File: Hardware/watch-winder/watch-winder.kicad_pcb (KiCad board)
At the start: 2 copper layers, 53 parts, among them J1 SWD, J2 UART, J3 MOT, J4 SYNC0, J5 SYNC1, J6 PWR, SW1 SW_Push, SW2 SW_Push, SW3 SW_Push, U1 STM32F030K6Tx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

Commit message: add pcb cutout, set 4 layer stackup
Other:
- board outline added: 50 x 50 mm
- copper layers 2 -> 4
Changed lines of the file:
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@@
 	(layers
 		(0 "F.Cu" signal)
+		(4 "In1.Cu" signal)
+		(6 "In2.Cu" signal)
 		(2 "B.Cu" signal)
 		(9 "F.Adhes" user "F.Adhesive")
@@
 	)
 	(setup
+		(stackup
+			(layer "F.SilkS"
+				(type "Top Silk Screen")
+			)
+			(layer "F.Paste"
+				(type "Top Solder Paste")
+			)
+			(layer "F.Mask"
+				(type "Top Solder Mask")
+				(thickness 0.01)
+			)
+			(layer "F.Cu"
+				(type "copper")
+				(thickness 0.035)
+			)
+			(layer "dielectric 1"
+				(type "prepreg")
+				(thickness 0.21)
+				(material "FR4")
+				(epsilon_r 4.5)
+				(loss_tangent 0.02)
+			)
+			(layer "In1.Cu"
+				(type "copper")
+				(thickness 0.015)
+			)
+			(layer "dielectric 2"
+				(type "core")
+				(thickness 1.06)
+				(material "FR4")
+				(epsilon_r 4.5)
+				(loss_tangent 0.02)
+			)
+			(layer "In2.Cu"
+				(type "copper")
+				(thickness 0.015)
+			)
+			(layer "dielectric 3"
+				(type "prepreg")
+				(thickness 0.21)
+				(material "FR4")
+				(epsilon_r 4.5)
+				(loss_tangent 0.02)
+			)
+			(layer "B.Cu"
+				(type "copper")
+				(thickness 0.035)
+			)
+			(layer "B.Mask"
+				(type "Bottom Solder Mask")
+				(thickness 0.01)
+			)
+			(layer "B.Paste"
+				(type "Bottom Solder Paste")
+			)
+			(layer "B.SilkS"
+				(type "Bottom Silk Screen")
+			)
+			(copper_finish "None")
+			(dielectric_constraints no)
+		)
 		(pad_to_mask_clearance 0)
 		(allow_soldermask_bridges_in_footprints no)
@@
 		)
 	)
+	(gr_rect
+		(start 160 100)
+		(end 210 150)
+		(stroke
+			(width 0.05)
+			(type default)
+		)
+		(fill no)
+		(layer "Edge.Cuts")
+	)
 	(embedded_fonts no)

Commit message: add gnd planes
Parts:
- moved J1 4.44 mm to (227.9, 102.7)
- moved J2 4.44 mm to (227.9, 114.9)
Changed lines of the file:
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@@
 	(footprint "Connector_PinHeader_2.54mm:PinHeader_1x04_P2.54mm_Horizontal"
 		(layer "F.Cu")
-		(at 227.87 119.355)
+		(at 227.87 114.92)
 		(descr "Through hole angled pin header, 1x04, 2.54mm pitch, 6mm pin length, single row")
 		(tags "Through hole angled pin header THT 1x04 2.54mm single row")
@@
 	(footprint "Connector_PinHeader_2.54mm:PinHeader_1x04_P2.54mm_Horizontal"
 		(layer "F.Cu")
-		(at 227.87 107.105)
+		(at 227.87 102.67)
 		(descr "Through hole angled pin header, 1x04, 2.54mm pitch, 6mm pin length, single row")
 		(tags "Through hole angled pin header THT 1x04 2.54mm single row")
@@
 	)
 	(gr_rect
+		(start 160 100)
+		(end 210 150)
+		(stroke
+			(width 0.2)
+			(type solid)
+		)
+		(fill yes)
+		(layer "In1.Cu")
+		(net 1)
+	)
+	(gr_rect
+		(start 160 100)
+		(end 210 150)
+		(stroke
+			(width 0.2)
+			(type solid)
+		)
+		(fill yes)
+		(layer "In2.Cu")
+		(net 1)
+	)
+	(gr_rect

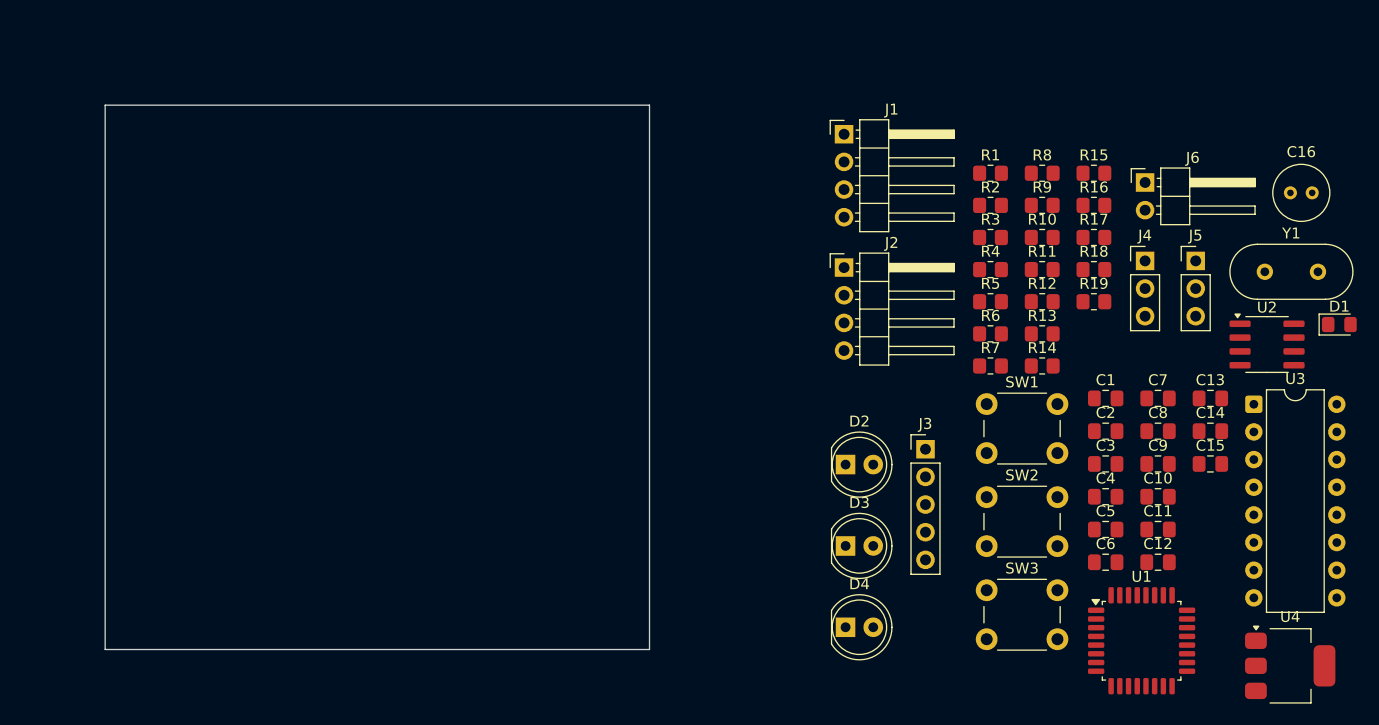
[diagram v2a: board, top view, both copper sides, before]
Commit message: start button/led placement
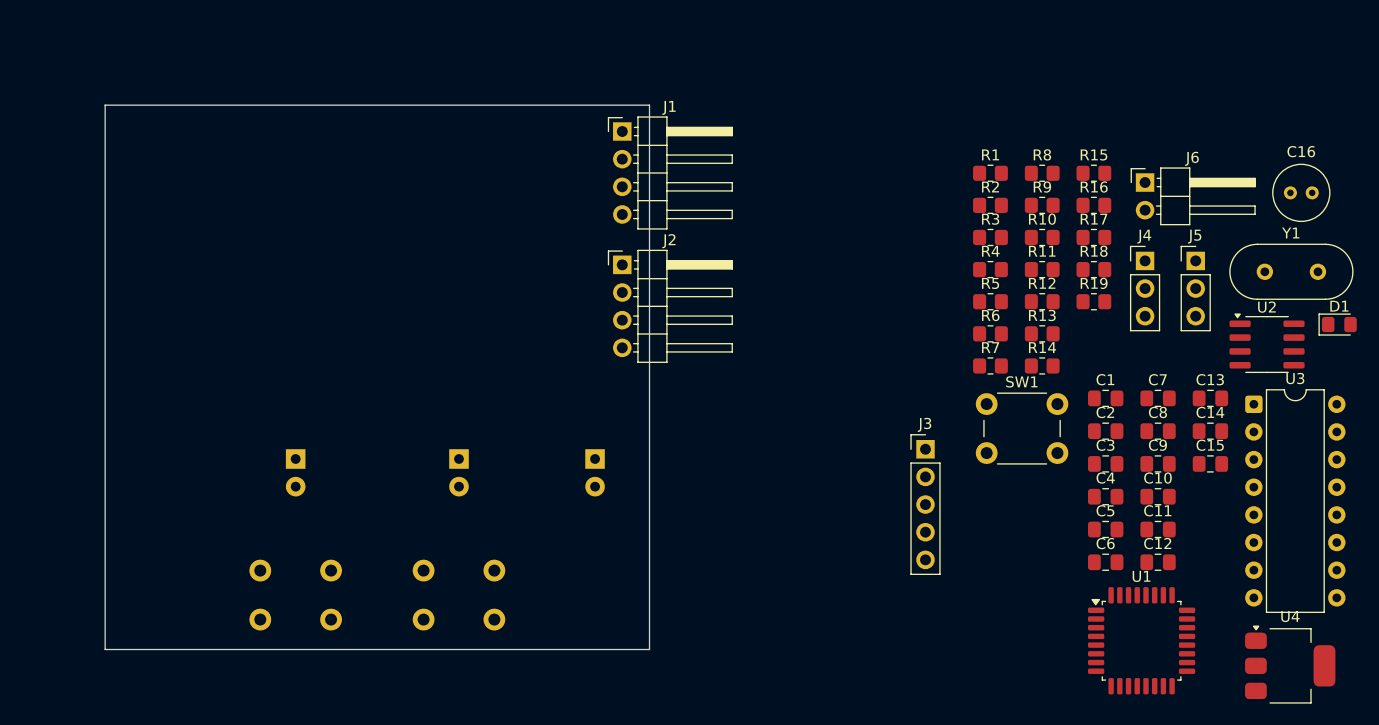
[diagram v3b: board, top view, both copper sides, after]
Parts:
- D2, D3, D4, SW2, SW3: moved to B.Cu
- moved SW3 66.8 mm to (174.2, 147.2)
- moved SW2 52.9 mm to (189.2, 147.2)
- moved D2 50.5 mm to (177.5, 132.5), turned to -90 degrees
- moved D3 36.4 mm to (192.5, 132.5), turned to -90 degrees
- moved D4 27.7 mm to (205.0, 132.5), turned to -90 degrees
- moved J1 20.4 mm to (207.5, 102.4)
- moved J2 20.4 mm to (207.5, 114.7)

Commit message: fix gnd, more components
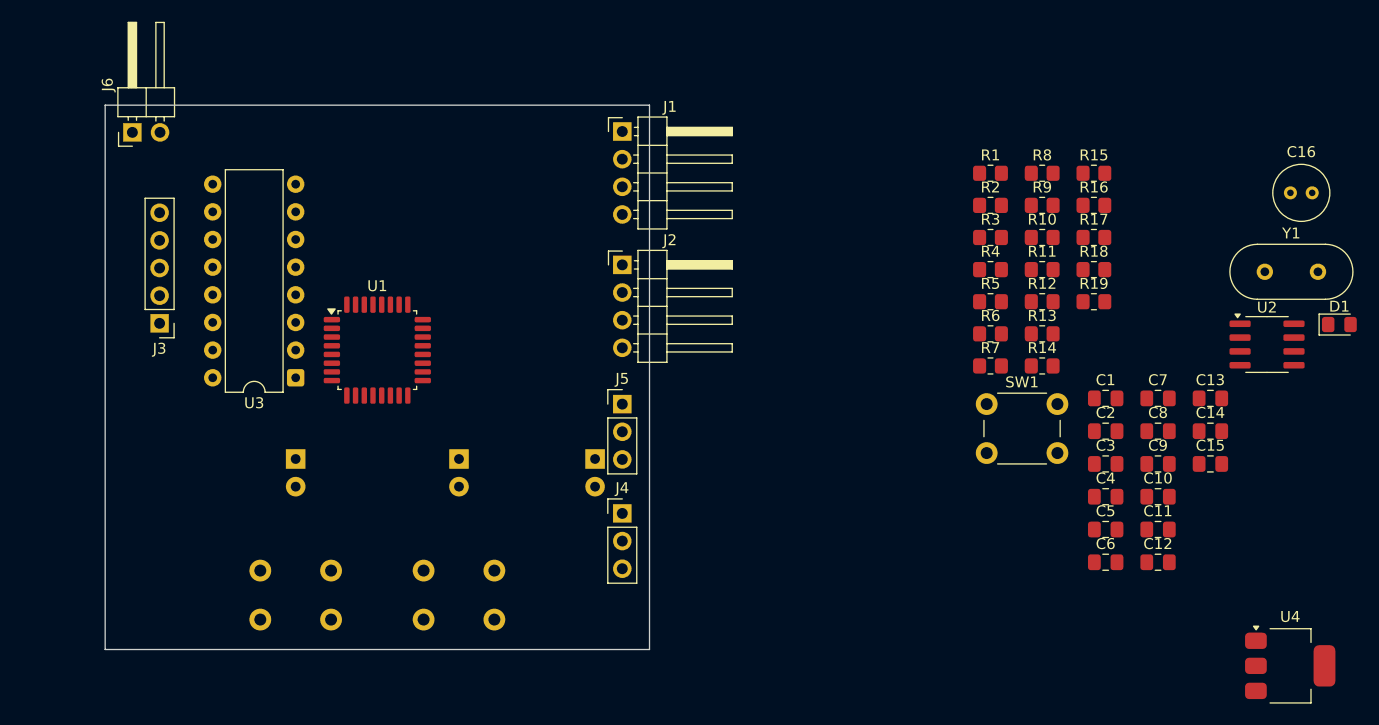
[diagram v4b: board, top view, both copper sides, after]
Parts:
- moved J6 93.1 mm to (162.5, 102.5), turned to 90 degrees
- moved U3 88.0 mm to (177.5, 125.0), turned to 180 degrees
- moved U1 75.1 mm to (185.0, 122.5)
- moved J3 71.3 mm to (165.0, 120.0), turned to 180 degrees
- moved J5 54.3 mm to (207.5, 127.5)
- moved J4 53.3 mm to (207.5, 137.5)
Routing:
- added copper zone on In1.Cu, net GND
- added copper zone on In2.Cu, net GND

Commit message: better placement
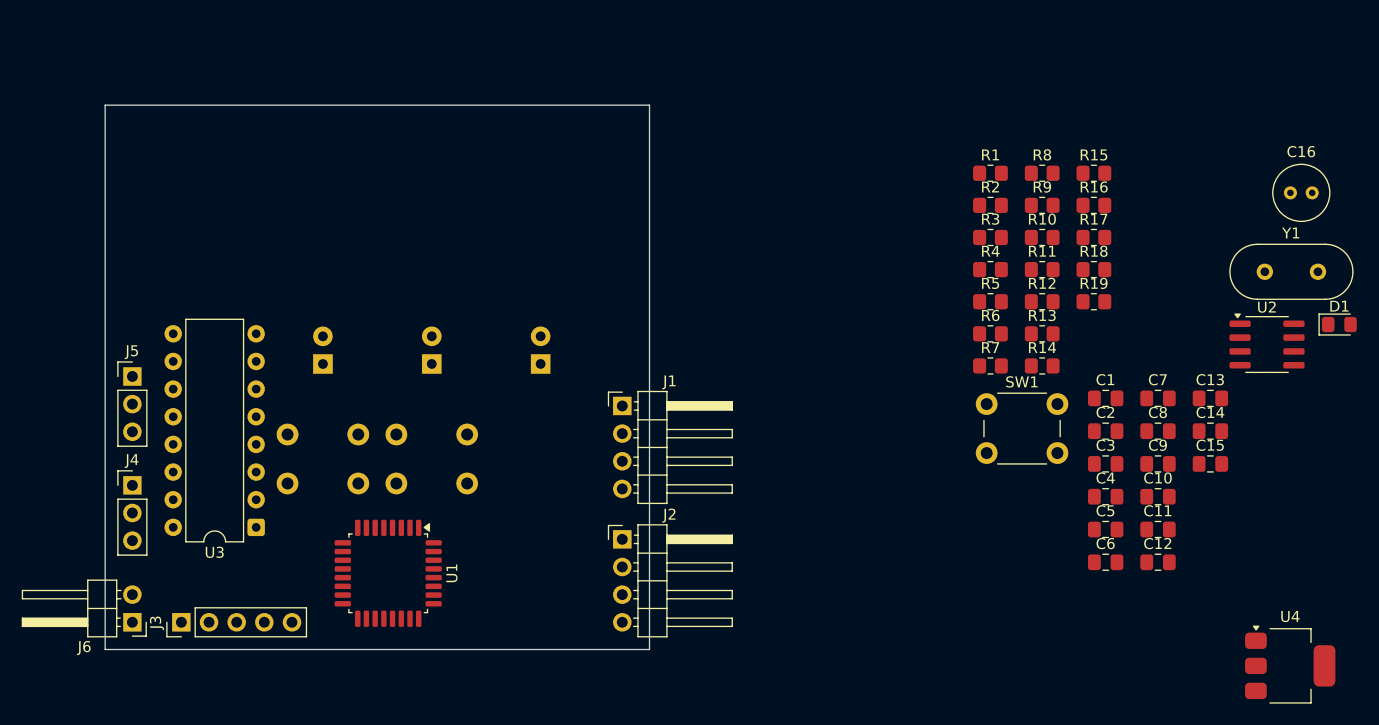
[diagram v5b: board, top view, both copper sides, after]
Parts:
- moved J4 45.1 mm to (162.5, 134.9)
- moved J5 45.1 mm to (162.5, 124.9)
- moved J6 45.0 mm to (162.5, 147.5), turned to 180 degrees
- moved J3 27.5 mm to (167.0, 147.5), turned to 90 degrees
- moved J1 25.2 mm to (207.5, 127.6)
- moved J2 25.2 mm to (207.5, 139.9)
- moved U1 20.5 mm to (186.0, 143.0), turned to -90 degrees
- moved SW3 19.2 mm to (183.2, 130.2), turned to 180 degrees
- moved SW2 17.5 mm to (193.2, 130.2), turned to 180 degrees
- moved U3 14.2 mm to (173.9, 138.8)
- moved D4 10.1 mm to (200.0, 123.8), turned to 90 degrees
- moved D3 9.08 mm to (190.0, 123.8), turned to 90 degrees
- moved D2 9.08 mm to (180.0, 123.8), turned to 90 degrees

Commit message: more or less final placement
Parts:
- moved C16 106.4 mm to (167.2, 139.4)
- moved U4 92.4 mm to (177.2, 140.2)
- moved C15 91.2 mm to (170.9, 143.2), turned to 180 degrees
- moved C11 89.7 mm to (167.1, 143.2)
- moved R10 86.7 mm to (163.3, 138.1)
- moved R12 85.7 mm to (163.3, 140.3), turned to 180 degrees
- moved C14 84.7 mm to (176.9, 134.5), turned to 90 degrees
- moved R11 83.5 mm to (163.2, 125.3), turned to 180 degrees
- moved R13 83.1 mm to (163.2, 127.2), turned to 180 degrees
- moved C13 82.5 mm to (179.0, 125.9), turned to 90 degrees
- moved C10 82.2 mm to (176.4, 118.2), turned to -90 degrees
- moved Y1 81.0 mm to (188.0, 135.0)
- moved D1 79.5 mm to (198.9, 148.0), turned to 180 degrees
- moved C12 78.6 mm to (179.0, 130.3), turned to 90 degrees
- moved C8 74.3 mm to (182.5, 133.5), turned to 180 degrees
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
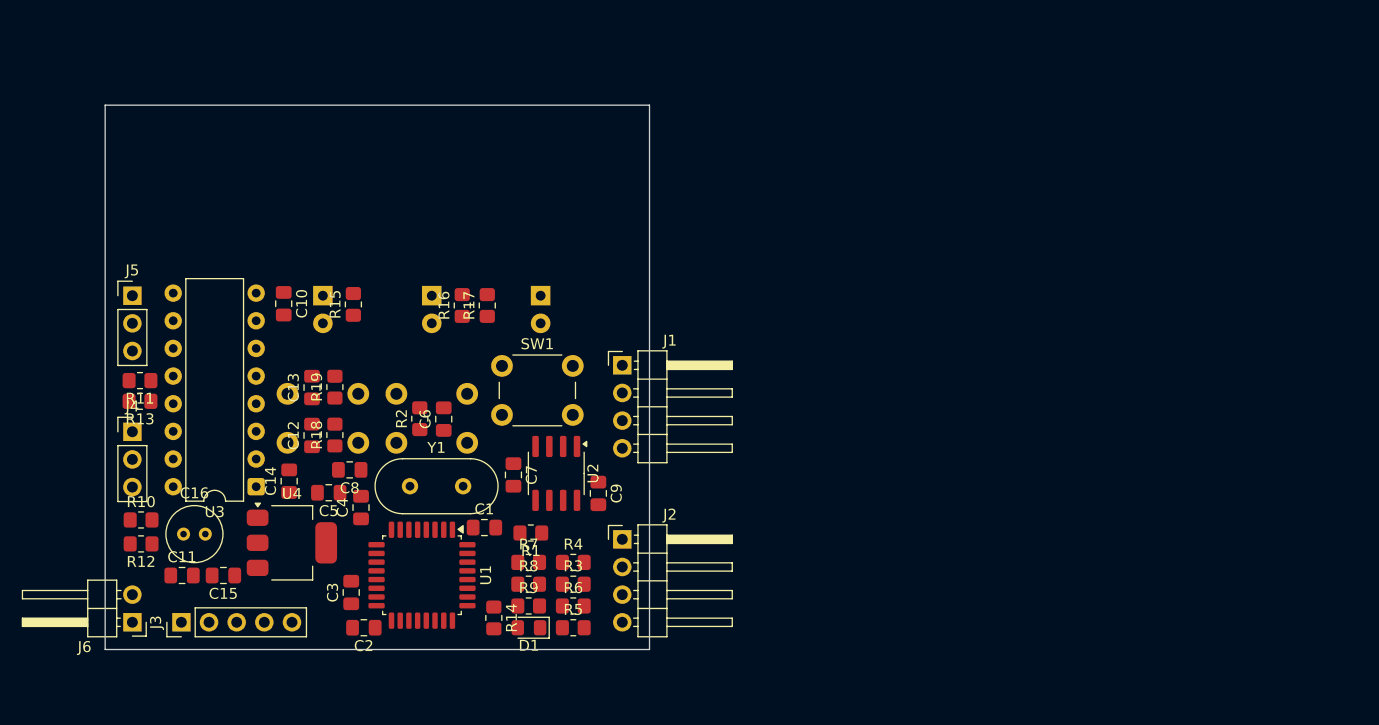
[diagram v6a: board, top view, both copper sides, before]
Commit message: lower board size, add mounting holes
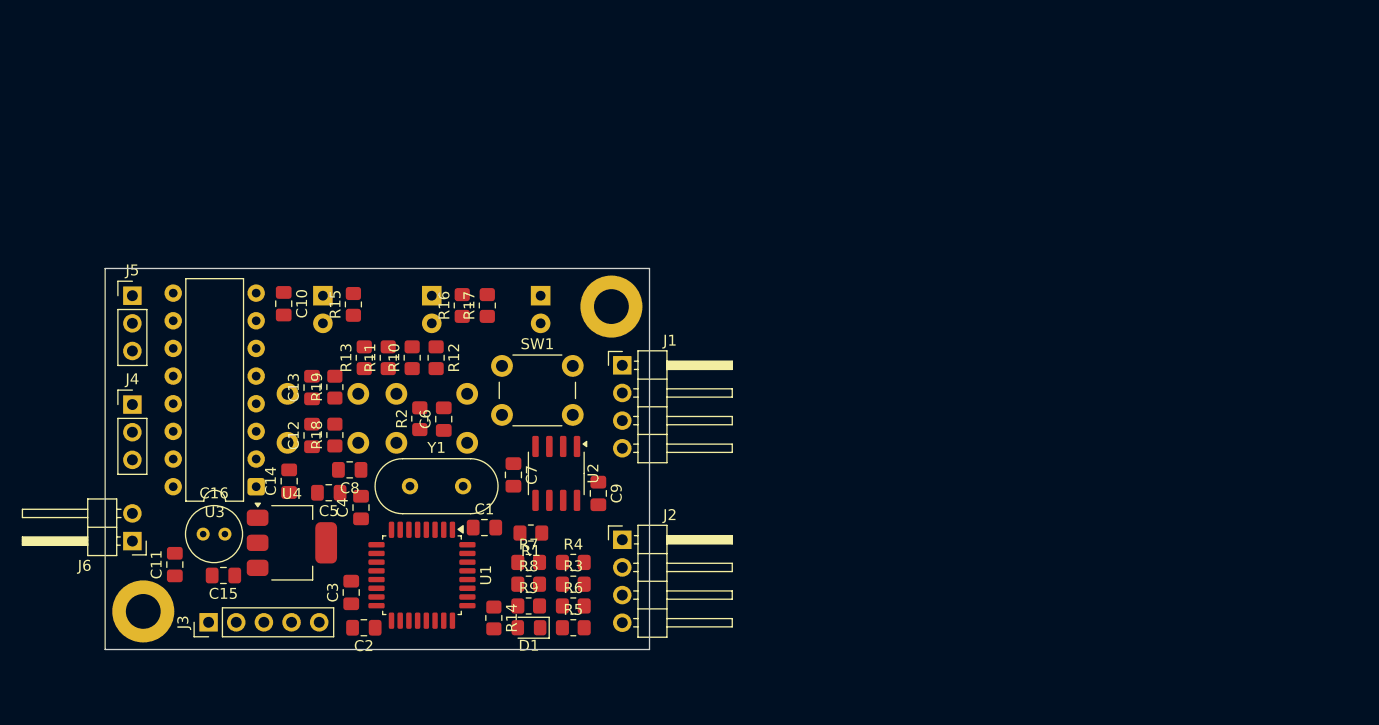
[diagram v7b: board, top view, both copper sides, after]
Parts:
- added REF**: MountingHole_3.2mm_M3_ISO7380_Pad, MountingHole:MountingHole_3.2mm_M3_ISO7380_Pad, F.Cu at (206.5, 118.5)
- added REF**: MountingHole_3.2mm_M3_ISO7380_Pad, MountingHole:MountingHole_3.2mm_M3_ISO7380_Pad, F.Cu at (163.5, 146.5)
- moved R12 32.0 mm to (190.4, 123.2), turned to -90 degrees
- moved R10 29.0 mm to (188.2, 123.2), turned to 90 degrees
- moved R11 22.9 mm to (186.0, 123.2), turned to 90 degrees
- moved R13 21.0 mm to (183.8, 123.2), turned to 90 degrees
- moved J6 7.46 mm to (162.5, 140.0)
- moved J3 2.50 mm to (169.5, 147.5)
- moved J4 2.50 mm to (162.5, 127.5)
- moved C16 1.80 mm to (169.0, 139.4)
- moved C11 1.20 mm to (166.4, 142.2), turned to 90 degrees
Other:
- board size 50 x 50 mm -> 50 x 35 mm

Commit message: add third mounting hole
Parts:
- added REF**: MountingHole_3.2mm_M3_ISO7380_Pad, MountingHole:MountingHole_3.2mm_M3_ISO7380_Pad, F.Cu at (207.0, 147.0)
- J2: footprint Connector_PinHeader_2.54mm:PinHeader_1x04_P2.54mm_Horizontal -> Connector_PinHeader_2.54mm:PinHeader_1x03_P2.54mm_Vertical
- moved C9 4.11 mm to (202.6, 138.8), turned to 180 degrees
- moved J2 3.92 mm to (207.5, 136.0)
- moved R5 1.80 mm to (202.0, 146.5)
- moved R6 1.72 mm to (202.0, 144.6)
- moved R9 1.66 mm to (198.0, 144.6)
- moved R3 1.64 mm to (202.0, 142.7)
- moved R8 1.58 mm to (198.0, 142.7)
- moved R4 1.56 mm to (202.0, 140.8)
- moved R7 1.50 mm to (198.0, 140.8)
- moved R14 0.95 mm to (196.6, 147.4)
- moved R1 0.58 mm to (198.8, 138.8)
- moved D1 0.58 mm to (198.9, 147.4), turned to 90 degrees
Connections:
- J4 pad 1: +5V -> GND
- J4 pad 3: GND -> +5V
- J5 pad 1: +5V -> GND
- J5 pad 3: GND -> +5V
- J6 pad 1: +5V -> GND
- J6 pad 2: GND -> +5V
- R5 pad 2: Net-(J2-Pin_3) -> Net-(J2-Pin_2)
- R6 pad 2: Net-(J2-Pin_2) -> Net-(J2-Pin_3)
